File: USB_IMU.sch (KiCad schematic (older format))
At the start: 12 parts

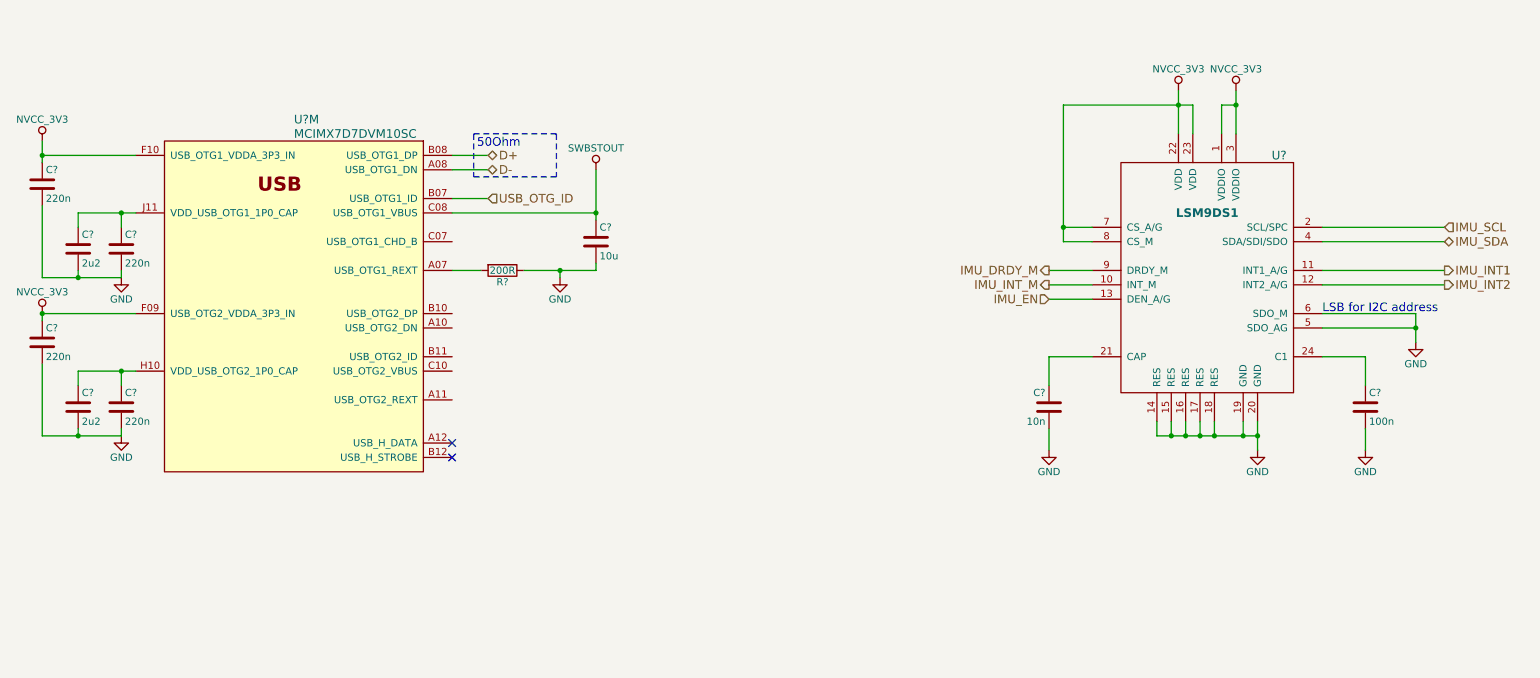
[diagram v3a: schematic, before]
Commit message: Prepare for two battery types NiMH battery for using the original battery pack LiPo battery for using long lasting modern battery
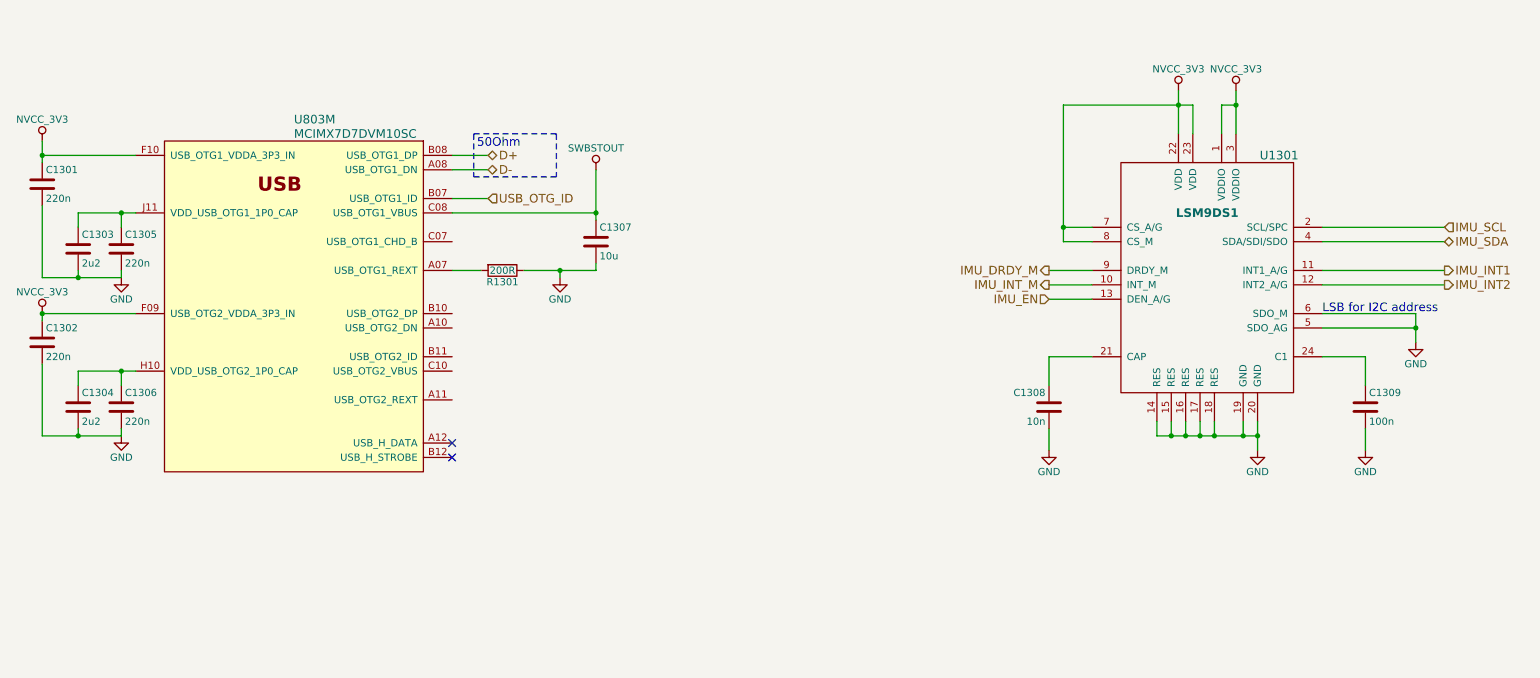
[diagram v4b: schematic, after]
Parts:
- gave numbers to parts that had none: 12
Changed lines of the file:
@@
 EESchema Schematic File Version 2
-LIBS:3210retro-rescue
-LIBS:power
-LIBS:device
-LIBS:transistors
-LIBS:conn
-LIBS:linear
-LIBS:regul
-LIBS:74xx
-LIBS:cmos4000
-LIBS:adc-dac
-LIBS:memory
-LIBS:xilinx
-LIBS:microcontrollers
-LIBS:dsp
-LIBS:microchip
-LIBS:analog_switches
-LIBS:motorola
-LIBS:texas
-LIBS:intel
-LIBS:audio
-LIBS:interface
-LIBS:digital-audio
-LIBS:philips
-LIBS:display
-LIBS:cypress
-LIBS:siliconi
-LIBS:opto
-LIBS:atmel
-LIBS:contrib
-LIBS:valves
 LIBS:a7
 LIBS:ft232rl
@@
 LIBS:sn74avc2t244
 LIBS:lsm9ds1
+LIBS:WM8960CGEFL
+LIBS:tps61021a
+LIBS:bq24400
+LIBS:power
+LIBS:device
+LIBS:transistors
+LIBS:conn
+LIBS:linear
+LIBS:regul
+LIBS:74xx
+LIBS:cmos4000
+LIBS:adc-dac
+LIBS:memory
+LIBS:xilinx
+LIBS:microcontrollers
+LIBS:dsp
+LIBS:microchip
+LIBS:analog_switches
+LIBS:motorola
+LIBS:texas
+LIBS:intel
+LIBS:audio
+LIBS:interface
+LIBS:digital-audio
+LIBS:philips
+LIBS:display
+LIBS:cypress
+LIBS:siliconi
+LIBS:opto
+LIBS:atmel
+LIBS:contrib
+LIBS:valves
 LIBS:3210retro-cache
 EELAYER 25 0
@@
 P 5650 3100
 AR Path="/5805F47D/594C5FFB" Ref="U?"  Part="13"
-AR Path="/5805F47D/594C5B6F/594C5FFB" Ref="U?"  Part="13"
-F 0 "U?" H 5650 3100 60  0000 L CNN
+AR Path="/5805F47D/594C5B6F/594C5FFB" Ref="U803"  Part="13"
+F 0 "U803" H 5650 3100 60  0000 L CNN
 F 1 "MCIMX7D7DVM10SC" H 5650 3000 60  0000 L CNN
 F 2 "" H 3400 4800 60  0001 C CNN
@@
 	7000 3650 6750 3650
 $Comp
-L SWBSTOUT #PWR?
+L SWBSTOUT #PWR1306
 U 1 1 594C6005
 P 7750 3450
-F 0 "#PWR?" H 7750 3300 50  0001 C CNN
+F 0 "#PWR1306" H 7750 3300 50  0001 C CNN
 F 1 "SWBSTOUT" H 7750 3600 50  0000 C CNN
 F 2 "" H 7750 3450 50  0001 C CNN
@@
 	7750 3750 6750 3750
 $Comp
-L R R?
+L R R1301
 U 1 1 594C600E
 P 7100 4150
-F 0 "R?" V 7180 4150 50  0000 C CNN
+F 0 "R1301" V 7180 4150 50  0000 C CNN
 F 1 "200R" V 7100 4150 50  0000 C CNN
 F 2 "" V 7030 4150 50  0000 C CNN
@@
 	7500 4150 7500 4200
 $Comp
-L GND #PWR?
+L GND #PWR1305
 U 1 1 594C6019
 P 7500 4200
-F 0 "#PWR?" H 7500 3950 50  0001 C CNN
+F 0 "#PWR1305" H 7500 3950 50  0001 C CNN
 F 1 "GND" H 7500 4050 50  0000 C CNN
 F 2 "" H 7500 4200 50  0000 C CNN
@@
 $EndComp
 $Comp
-L C C?
+L C C1307
 U 1 1 594C601F
 P 7750 3950
-F 0 "C?" H 7775 4050 50  0000 L CNN
+F 0 "C1307" H 7775 4050 50  0000 L CNN
 F 1 "10u" H 7775 3850 50  0000 L CNN
 F 2 "" H 7788 3800 50  0000 C CNN
@@
 NoConn ~ 6750 5450
 $Comp
-L NVCC_3V3 #PWR?
+L NVCC_3V3 #PWR1301
 U 1 1 594C602B
 P 3900 3250
-F 0 "#PWR?" H 3900 3100 50  0001 C CNN
+F 0 "#PWR1301" H 3900 3100 50  0001 C CNN
 F 1 "NVCC_3V3" H 3900 3400 50  0000 C CNN
 F 2 "" H 3900 3250 50  0001 C CNN
@@
 	3900 3250 3900 3400
 $Comp
-L C C?
+L C C1301
 U 1 1 594C6034
 P 3900 3550
-F 0 "C?" H 3925 3650 50  0000 L CNN
+F 0 "C1301" H 3925 3650 50  0000 L CNN
 F 1 "220n" H 3925 3450 50  0000 L CNN
 F 2 "" H 3938 3400 50  0000 C CNN
@@
 Connection ~ 3900 3350
 $Comp
-L GND #PWR?
+L GND #PWR1303
 U 1 1 594C603C
 P 4450 4200
-F 0 "#PWR?" H 4450 3950 50  0001 C CNN
+F 0 "#PWR1303" H 4450 3950 50  0001 C CNN
 F 1 "GND" H 4450 4050 50  0000 C CNN
 F 2 "" H 4450 4200 50  0000 C CNN
@@
 $EndComp
 $Comp
-L C C?
+L C C1305
 U 1 1 594C6042
 P 4450 4000
-F 0 "C?" H 4475 4100 50  0000 L CNN
+F 0 "C1305" H 4475 4100 50  0000 L CNN
 F 1 "220n" H 4475 3900 50  0000 L CNN
 F 2 "" H 4488 3850 50  0000 C CNN
@@
 $EndComp
 $Comp
-L C C?
+L C C1303
 U 1 1 594C6049
 P 4150 4000
-F 0 "C?" H 4175 4100 50  0000 L CNN
+F 0 "C1303" H 4175 4100 50  0000 L CNN
 F 1 "2u2" H 4175 3900 50  0000 L CNN
 F 2 "" H 4188 3850 50  0000 C CNN
@@
 Connection ~ 4450 3750
 $Comp
-L NVCC_3V3 #PWR?
+L NVCC_3V3 #PWR1302
 U 1 1 594C605B
 P 3900 4450
-F 0 "#PWR?" H 3900 4300 50  0001 C CNN
+F 0 "#PWR1302" H 3900 4300 50  0001 C CNN
 F 1 "NVCC_3V3" H 3900 4600 50  0000 C CNN
 F 2 "" H 3900 4450 50  0001 C CNN
@@
 	3900 4450 3900 4500
 $Comp
-L C C?
+L C C1302
 U 1 1 594C6063
 P 3900 4650
-F 0 "C?" H 3925 4750 50  0000 L CNN
+F 0 "C1302" H 3925 4750 50  0000 L CNN
 F 1 "220n" H 3925 4550 50  0000 L CNN
 F 2 "" H 3938 4500 50  0000 C CNN
@@
 Connection ~ 3900 4450
 $Comp
-L GND #PWR?
+L GND #PWR1304
 U 1 1 594C606B
 P 4450 5300
-F 0 "#PWR?" H 4450 5050 50  0001 C CNN
+F 0 "#PWR1304" H 4450 5050 50  0001 C CNN
 F 1 "GND" H 4450 5150 50  0000 C CNN
 F 2 "" H 4450 5300 50  0000 C CNN
@@
 $EndComp
 $Comp
-L C C?
+L C C1306
 U 1 1 594C6071
 P 4450 5100
-F 0 "C?" H 4475 5200 50  0000 L CNN
+F 0 "C1306" H 4475 5200 50  0000 L CNN
 F 1 "220n" H 4475 5000 50  0000 L CNN
 F 2 "" H 4488 4950 50  0000 C CNN
@@
 $EndComp
 $Comp
-L C C?
+L C C1304
 U 1 1 594C6078
 P 4150 5100
-F 0 "C?" H 4175 5200 50  0000 L CNN
+F 0 "C1304" H 4175 5200 50  0000 L CNN
 F 1 "2u2" H 4175 5000 50  0000 L CNN
 F 2 "" H 4188 4950 50  0000 C CNN
@@
 IMU_SCL
 $Comp
-L LSM9DS1 U?
+L LSM9DS1 U1301
 U 1 1 5942F947
 P 12000 4350
-F 0 "U?" H 12500 5350 60  0000 C CNN
+F 0 "U1301" H 12500 5350 60  0000 C CNN
 F 1 "LSM9DS1" H 12000 4950 60  0000 C CNB
 F 2 "" H 12000 4350 60  0001 C CNN
@@
 Connection ~ 11750 5300
 $Comp
-L GND #PWR?
+L GND #PWR1310
 U 1 1 5942FEDE
 P 12350 5400
-F 0 "#PWR?" H 12350 5150 50  0001 C CNN
+F 0 "#PWR1310" H 12350 5150 50  0001 C CNN
 F 1 "GND" H 12350 5250 50  0000 C CNN
 F 2 "" H 12350 5400 50  0000 C CNN
@@
 LSB for I2C address
 $Comp
-L GND #PWR?
+L GND #PWR1312
 U 1 1 59430085
 P 13450 4650
-F 0 "#PWR?" H 13450 4400 50  0001 C CNN
+F 0 "#PWR1312" H 13450 4400 50  0001 C CNN
 F 1 "GND" H 13450 4500 50  0000 C CNN
 F 2 "" H 13450 4650 50  0000 C CNN
@@
 IMU_EN
 $Comp
-L C C?
+L C C1309
 U 1 1 59430293
 P 13100 5100
-F 0 "C?" H 13125 5200 50  0000 L CNN
+F 0 "C1309" H 13125 5200 50  0000 L CNN
 F 1 "100n" H 13125 5000 50  0000 L CNN
 F 2 "" H 13138 4950 50  0000 C CNN
@@
 	13100 4750 12800 4750
 $Comp
-L GND #PWR?
+L GND #PWR1311
 U 1 1 594303C6
 P 13100 5400
-F 0 "#PWR?" H 13100 5150 50  0001 C CNN
+F 0 "#PWR1311" H 13100 5150 50  0001 C CNN
 F 1 "GND" H 13100 5250 50  0000 C CNN
 F 2 "" H 13100 5400 50  0000 C CNN
@@
 	13100 5400 13100 5250
 $Comp
-L C C?
+L C C1308
 U 1 1 594304C7
 P 10900 5100
-F 0 "C?" H 10925 5200 50  0000 L CNN
+F 0 "C1308" H 10925 5200 50  0000 L CNN
 F 1 "10n" H 10925 5000 50  0000 L CNN
 F 2 "" H 10938 4950 50  0000 C CNN
@@
 	10900 4750 11200 4750
 $Comp
-L GND #PWR?
+L GND #PWR1307
 U 1 1 594304CF
 P 10900 5400
-F 0 "#PWR?" H 10900 5150 50  0001 C CNN
+F 0 "#PWR1307" H 10900 5150 50  0001 C CNN
 F 1 "GND" H 10900 5250 50  0000 C CNN
 F 2 "" H 10900 5400 50  0000 C CNN
@@
 	10900 5400 10900 5250
 $Comp
-L NVCC_3V3 #PWR?
+L NVCC_3V3 #PWR1308
 U 1 1 59430571
 P 11800 2900
-F 0 "#PWR?" H 11800 2750 50  0001 C CNN
+F 0 "#PWR1308" H 11800 2750 50  0001 C CNN
 F 1 "NVCC_3V3" H 11800 3050 50  0000 C CNN
 F 2 "" H 11800 2900 50  0001 C CNN
@@
 Connection ~ 12200 3000
 $Comp
-L NVCC_3V3 #PWR?
+L NVCC_3V3 #PWR1309
 U 1 1 59430BB5
 P 12200 2900
-F 0 "#PWR?" H 12200 2750 50  0001 C CNN
+F 0 "#PWR1309" H 12200 2750 50  0001 C CNN
 F 1 "NVCC_3V3" H 12200 3050 50  0000 C CNN
 F 2 "" H 12200 2900 50  0001 C CNN

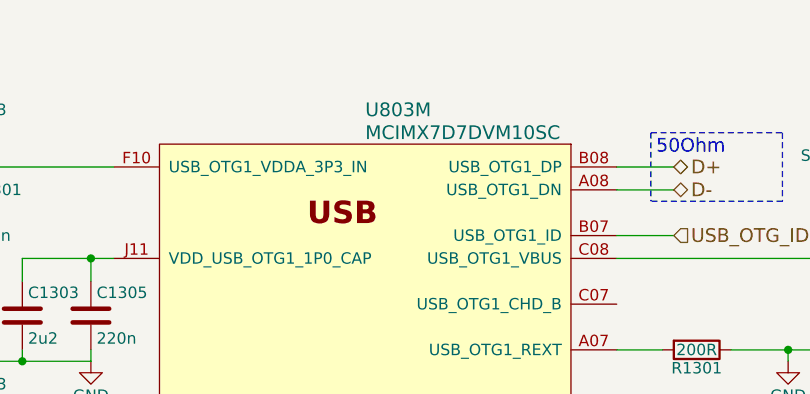
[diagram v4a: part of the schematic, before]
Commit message: Changed several voltage rail connections Removed non existing rails Added circuit for NiMH charging
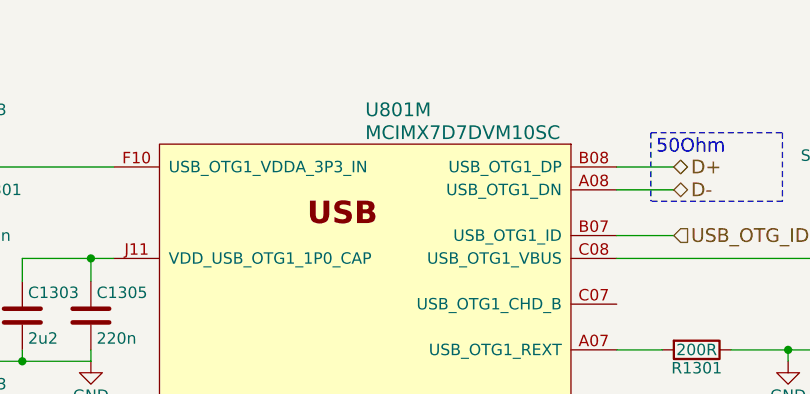
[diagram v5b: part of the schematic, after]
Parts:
- renumbered U803 to U801
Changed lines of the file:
@@
 P 5650 3100
 AR Path="/5805F47D/594C5FFB" Ref="U?"  Part="13"
-AR Path="/5805F47D/594C5B6F/594C5FFB" Ref="U803"  Part="13"
-F 0 "U803" H 5650 3100 60  0000 L CNN
+AR Path="/5805F47D/594C5B6F/594C5FFB" Ref="U801"  Part="13"
+F 0 "U801" H 5650 3100 60  0000 L CNN
 F 1 "MCIMX7D7DVM10SC" H 5650 3000 60  0000 L CNN
 F 2 "" H 3400 4800 60  0001 C CNN
@@
 	7000 3650 6750 3650
 $Comp
-L SWBSTOUT #PWR1306
+L SWBSTOUT #PWR0300
 U 1 1 594C6005
 P 7750 3450
-F 0 "#PWR1306" H 7750 3300 50  0001 C CNN
+F 0 "#PWR0300" H 7750 3300 50  0001 C CNN
 F 1 "SWBSTOUT" H 7750 3600 50  0000 C CNN
 F 2 "" H 7750 3450 50  0001 C CNN
@@
 	7500 4150 7500 4200
 $Comp
-L GND #PWR1305
+L GND #PWR0301
 U 1 1 594C6019
 P 7500 4200
-F 0 "#PWR1305" H 7500 3950 50  0001 C CNN
+F 0 "#PWR0301" H 7500 3950 50  0001 C CNN
 F 1 "GND" H 7500 4050 50  0000 C CNN
 F 2 "" H 7500 4200 50  0000 C CNN
@@
 NoConn ~ 6750 5450
 $Comp
-L NVCC_3V3 #PWR1301
+L NVCC_3V3 #PWR0302
 U 1 1 594C602B
 P 3900 3250
-F 0 "#PWR1301" H 3900 3100 50  0001 C CNN
+F 0 "#PWR0302" H 3900 3100 50  0001 C CNN
 F 1 "NVCC_3V3" H 3900 3400 50  0000 C CNN
 F 2 "" H 3900 3250 50  0001 C CNN
@@
 Connection ~ 3900 3350
 $Comp
-L GND #PWR1303
+L GND #PWR0303
 U 1 1 594C603C
 P 4450 4200
-F 0 "#PWR1303" H 4450 3950 50  0001 C CNN
+F 0 "#PWR0303" H 4450 3950 50  0001 C CNN
 F 1 "GND" H 4450 4050 50  0000 C CNN
 F 2 "" H 4450 4200 50  0000 C CNN
@@
 Connection ~ 4450 3750
 $Comp
-L NVCC_3V3 #PWR1302
+L NVCC_3V3 #PWR0304
 U 1 1 594C605B
 P 3900 4450
-F 0 "#PWR1302" H 3900 4300 50  0001 C CNN
+F 0 "#PWR0304" H 3900 4300 50  0001 C CNN
 F 1 "NVCC_3V3" H 3900 4600 50  0000 C CNN
 F 2 "" H 3900 4450 50  0001 C CNN
@@
 Connection ~ 3900 4450
 $Comp
-L GND #PWR1304
+L GND #PWR0305
 U 1 1 594C606B
 P 4450 5300
-F 0 "#PWR1304" H 4450 5050 50  0001 C CNN
+F 0 "#PWR0305" H 4450 5050 50  0001 C CNN
 F 1 "GND" H 4450 5150 50  0000 C CNN
 F 2 "" H 4450 5300 50  0000 C CNN
@@
 Connection ~ 11750 5300
 $Comp
-L GND #PWR1310
+L GND #PWR0306
 U 1 1 5942FEDE
 P 12350 5400
-F 0 "#PWR1310" H 12350 5150 50  0001 C CNN
+F 0 "#PWR0306" H 12350 5150 50  0001 C CNN
 F 1 "GND" H 12350 5250 50  0000 C CNN
 F 2 "" H 12350 5400 50  0000 C CNN
@@
 LSB for I2C address
 $Comp
-L GND #PWR1312
+L GND #PWR0307
 U 1 1 59430085
 P 13450 4650
-F 0 "#PWR1312" H 13450 4400 50  0001 C CNN
+F 0 "#PWR0307" H 13450 4400 50  0001 C CNN
 F 1 "GND" H 13450 4500 50  0000 C CNN
 F 2 "" H 13450 4650 50  0000 C CNN
@@
 	13100 4750 12800 4750
 $Comp
-L GND #PWR1311
+L GND #PWR0308
 U 1 1 594303C6
 P 13100 5400
-F 0 "#PWR1311" H 13100 5150 50  0001 C CNN
+F 0 "#PWR0308" H 13100 5150 50  0001 C CNN
 F 1 "GND" H 13100 5250 50  0000 C CNN
 F 2 "" H 13100 5400 50  0000 C CNN
@@
 	10900 4750 11200 4750
 $Comp
-L GND #PWR1307
+L GND #PWR0309
 U 1 1 594304CF
 P 10900 5400
-F 0 "#PWR1307" H 10900 5150 50  0001 C CNN
+F 0 "#PWR0309" H 10900 5150 50  0001 C CNN
 F 1 "GND" H 10900 5250 50  0000 C CNN
 F 2 "" H 10900 5400 50  0000 C CNN
@@
 	10900 5400 10900 5250
 $Comp
-L NVCC_3V3 #PWR1308
+L NVCC_3V3 #PWR0310
 U 1 1 59430571
 P 11800 2900
-F 0 "#PWR1308" H 11800 2750 50  0001 C CNN
+F 0 "#PWR0310" H 11800 2750 50  0001 C CNN
 F 1 "NVCC_3V3" H 11800 3050 50  0000 C CNN
 F 2 "" H 11800 2900 50  0001 C CNN
@@
 Connection ~ 12200 3000
 $Comp
-L NVCC_3V3 #PWR1309
+L NVCC_3V3 #PWR0311
 U 1 1 59430BB5
 P 12200 2900
-F 0 "#PWR1309" H 12200 2750 50  0001 C CNN
+F 0 "#PWR0311" H 12200 2750 50  0001 C CNN
 F 1 "NVCC_3V3" H 12200 3050 50  0000 C CNN
 F 2 "" H 12200 2900 50  0001 C CNN

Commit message: Created netlist with current components Foreward Annotation to Board
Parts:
- C1301, C1302, C1305, C1306, C1309: footprint (none) -> Capacitors_SMD:C_0402
- C1303, C1304, C1307, C1308: footprint (none) -> Capacitors_SMD:C_0603
- R1301: footprint (none) -> Resistors_SMD:R_0402
- U1301: footprint (none) -> NokiaRetroFit:LSM9DS1
- U801: footprint (none) -> NokiaRetroFit:BGA_541_075_19x19
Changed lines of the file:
@@
 F 0 "U801" H 5650 3100 60  0000 L CNN
 F 1 "MCIMX7D7DVM10SC" H 5650 3000 60  0000 L CNN
-F 2 "" H 3400 4800 60  0001 C CNN
+F 2 "NokiaRetroFit:BGA_541_075_19x19" H 3400 4800 60  0001 C CNN
 F 3 "" H 3400 4800 60  0001 C CNN
 	13   5650 3100
@@
 	7000 3650 6750 3650
 $Comp
-L SWBSTOUT #PWR0300
+L SWBSTOUT #PWR0299
 U 1 1 594C6005
 P 7750 3450
-F 0 "#PWR0300" H 7750 3300 50  0001 C CNN
+F 0 "#PWR0299" H 7750 3300 50  0001 C CNN
 F 1 "SWBSTOUT" H 7750 3600 50  0000 C CNN
 F 2 "" H 7750 3450 50  0001 C CNN
@@
 F 0 "R1301" V 7180 4150 50  0000 C CNN
 F 1 "200R" V 7100 4150 50  0000 C CNN
-F 2 "" V 7030 4150 50  0000 C CNN
+F 2 "Resistors_SMD:R_0402" V 7030 4150 50  0001 C CNN
 F 3 "" H 7100 4150 50  0000 C CNN
 	1    7100 4150
@@
 	7500 4150 7500 4200
 $Comp
-L GND #PWR0301
+L GND #PWR0300
 U 1 1 594C6019
 P 7500 4200
-F 0 "#PWR0301" H 7500 3950 50  0001 C CNN
+F 0 "#PWR0300" H 7500 3950 50  0001 C CNN
 F 1 "GND" H 7500 4050 50  0000 C CNN
 F 2 "" H 7500 4200 50  0000 C CNN
@@
 F 0 "C1307" H 7775 4050 50  0000 L CNN
 F 1 "10u" H 7775 3850 50  0000 L CNN
-F 2 "" H 7788 3800 50  0000 C CNN
+F 2 "Capacitors_SMD:C_0603" H 7788 3800 50  0001 C CNN
 F 3 "" H 7750 3950 50  0000 C CNN
 	1    7750 3950
@@
 NoConn ~ 6750 5450
 $Comp
-L NVCC_3V3 #PWR0302
+L NVCC_3V3 #PWR0301
 U 1 1 594C602B
 P 3900 3250
-F 0 "#PWR0302" H 3900 3100 50  0001 C CNN
+F 0 "#PWR0301" H 3900 3100 50  0001 C CNN
 F 1 "NVCC_3V3" H 3900 3400 50  0000 C CNN
 F 2 "" H 3900 3250 50  0001 C CNN
@@
 F 0 "C1301" H 3925 3650 50  0000 L CNN
 F 1 "220n" H 3925 3450 50  0000 L CNN
-F 2 "" H 3938 3400 50  0000 C CNN
+F 2 "Capacitors_SMD:C_0402" H 3938 3400 50  0001 C CNN
 F 3 "" H 3900 3550 50  0000 C CNN
 	1    3900 3550
@@
 Connection ~ 3900 3350
 $Comp
-L GND #PWR0303
+L GND #PWR0302
 U 1 1 594C603C
 P 4450 4200
-F 0 "#PWR0303" H 4450 3950 50  0001 C CNN
+F 0 "#PWR0302" H 4450 3950 50  0001 C CNN
 F 1 "GND" H 4450 4050 50  0000 C CNN
 F 2 "" H 4450 4200 50  0000 C CNN
@@
 F 0 "C1305" H 4475 4100 50  0000 L CNN
 F 1 "220n" H 4475 3900 50  0000 L CNN
-F 2 "" H 4488 3850 50  0000 C CNN
+F 2 "Capacitors_SMD:C_0402" H 4488 3850 50  0001 C CNN
 F 3 "" H 4450 4000 50  0000 C CNN
 	1    4450 4000
@@
 F 0 "C1303" H 4175 4100 50  0000 L CNN
 F 1 "2u2" H 4175 3900 50  0000 L CNN
-F 2 "" H 4188 3850 50  0000 C CNN
+F 2 "Capacitors_SMD:C_0603" H 4188 3850 50  0001 C CNN
 F 3 "" H 4150 4000 50  0000 C CNN
 	1    4150 4000
@@
 Connection ~ 4450 3750
 $Comp
-L NVCC_3V3 #PWR0304
+L NVCC_3V3 #PWR0303
 U 1 1 594C605B
 P 3900 4450
-F 0 "#PWR0304" H 3900 4300 50  0001 C CNN
+F 0 "#PWR0303" H 3900 4300 50  0001 C CNN
 F 1 "NVCC_3V3" H 3900 4600 50  0000 C CNN
 F 2 "" H 3900 4450 50  0001 C CNN
@@
 F 0 "C1302" H 3925 4750 50  0000 L CNN
 F 1 "220n" H 3925 4550 50  0000 L CNN
-F 2 "" H 3938 4500 50  0000 C CNN
+F 2 "Capacitors_SMD:C_0402" H 3938 4500 50  0001 C CNN
 F 3 "" H 3900 4650 50  0000 C CNN
 	1    3900 4650
@@
 Connection ~ 3900 4450
 $Comp
-L GND #PWR0305
+L GND #PWR0304
 U 1 1 594C606B
 P 4450 5300
-F 0 "#PWR0305" H 4450 5050 50  0001 C CNN
+F 0 "#PWR0304" H 4450 5050 50  0001 C CNN
 F 1 "GND" H 4450 5150 50  0000 C CNN
 F 2 "" H 4450 5300 50  0000 C CNN
@@
 F 0 "C1306" H 4475 5200 50  0000 L CNN
 F 1 "220n" H 4475 5000 50  0000 L CNN
-F 2 "" H 4488 4950 50  0000 C CNN
+F 2 "Capacitors_SMD:C_0402" H 4488 4950 50  0001 C CNN
 F 3 "" H 4450 5100 50  0000 C CNN
 	1    4450 5100
@@
 F 0 "C1304" H 4175 5200 50  0000 L CNN
 F 1 "2u2" H 4175 5000 50  0000 L CNN
-F 2 "" H 4188 4950 50  0000 C CNN
+F 2 "Capacitors_SMD:C_0603" H 4188 4950 50  0001 C CNN
 F 3 "" H 4150 5100 50  0000 C CNN
 	1    4150 5100
@@
 F 0 "U1301" H 12500 5350 60  0000 C CNN
 F 1 "LSM9DS1" H 12000 4950 60  0000 C CNB
-F 2 "" H 12000 4350 60  0001 C CNN
+F 2 "NokiaRetroFit:LSM9DS1" H 12000 4350 60  0001 C CNN
 F 3 "" H 12000 4350 60  0001 C CNN
 	1    12000 4350
@@
 Connection ~ 11750 5300
 $Comp
-L GND #PWR0306
+L GND #PWR0305
 U 1 1 5942FEDE
 P 12350 5400
-F 0 "#PWR0306" H 12350 5150 50  0001 C CNN
+F 0 "#PWR0305" H 12350 5150 50  0001 C CNN
 F 1 "GND" H 12350 5250 50  0000 C CNN
 F 2 "" H 12350 5400 50  0000 C CNN
@@
 LSB for I2C address
 $Comp
-L GND #PWR0307
+L GND #PWR0306
 U 1 1 59430085
 P 13450 4650
-F 0 "#PWR0307" H 13450 4400 50  0001 C CNN
+F 0 "#PWR0306" H 13450 4400 50  0001 C CNN
 F 1 "GND" H 13450 4500 50  0000 C CNN
 F 2 "" H 13450 4650 50  0000 C CNN
@@
 F 0 "C1309" H 13125 5200 50  0000 L CNN
 F 1 "100n" H 13125 5000 50  0000 L CNN
-F 2 "" H 13138 4950 50  0000 C CNN
+F 2 "Capacitors_SMD:C_0402" H 13138 4950 50  0001 C CNN
 F 3 "" H 13100 5100 50  0000 C CNN
 	1    13100 5100
@@
 	13100 4750 12800 4750
 $Comp
-L GND #PWR0308
+L GND #PWR0307
 U 1 1 594303C6
 P 13100 5400
-F 0 "#PWR0308" H 13100 5150 50  0001 C CNN
+F 0 "#PWR0307" H 13100 5150 50  0001 C CNN
 F 1 "GND" H 13100 5250 50  0000 C CNN
 F 2 "" H 13100 5400 50  0000 C CNN
@@
 F 0 "C1308" H 10925 5200 50  0000 L CNN
 F 1 "10n" H 10925 5000 50  0000 L CNN
-F 2 "" H 10938 4950 50  0000 C CNN
+F 2 "Capacitors_SMD:C_0603" H 10938 4950 50  0001 C CNN
 F 3 "" H 10900 5100 50  0000 C CNN
 	1    10900 5100
@@
 	10900 4750 11200 4750
 $Comp
-L GND #PWR0309
+L GND #PWR0308
 U 1 1 594304CF
 P 10900 5400
-F 0 "#PWR0309" H 10900 5150 50  0001 C CNN
+F 0 "#PWR0308" H 10900 5150 50  0001 C CNN
 F 1 "GND" H 10900 5250 50  0000 C CNN
 F 2 "" H 10900 5400 50  0000 C CNN
@@
 	10900 5400 10900 5250
 $Comp
-L NVCC_3V3 #PWR0310
+L NVCC_3V3 #PWR0309
 U 1 1 59430571
 P 11800 2900
-F 0 "#PWR0310" H 11800 2750 50  0001 C CNN
+F 0 "#PWR0309" H 11800 2750 50  0001 C CNN
 F 1 "NVCC_3V3" H 11800 3050 50  0000 C CNN
 F 2 "" H 11800 2900 50  0001 C CNN
@@
 Connection ~ 12200 3000
 $Comp
-L NVCC_3V3 #PWR0311
+L NVCC_3V3 #PWR0310
 U 1 1 59430BB5
 P 12200 2900
-F 0 "#PWR0311" H 12200 2750 50  0001 C CNN
+F 0 "#PWR0310" H 12200 2750 50  0001 C CNN
 F 1 "NVCC_3V3" H 12200 3050 50  0000 C CNN
 F 2 "" H 12200 2900 50  0001 C CNN
